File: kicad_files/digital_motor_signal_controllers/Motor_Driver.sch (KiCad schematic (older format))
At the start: 36 parts

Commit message: Code and PCB modifications
Adjustments to DSC motor controller PCB as well as BOMs
Nearly completed cannibalization of VESC code for the DSC motor control
application.
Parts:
- added D4: TVS, SMAJ5.0A:DIOM5026X229N, symbol SMAJ5.0A:SMAJ5.0A
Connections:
- net +5V: now also D4.1
- net GND: now also D4.2
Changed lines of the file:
@@
 EESchema Schematic File Version 4
 LIBS:DSC_motor_controller-cache
-EELAYER 26 0
+EELAYER 30 0
 EELAYER END
 $Descr A4 11693 8268
@@
 U 1 1 5D363539
 P 4650 2800
-F 0 "DRV1" H 4650 4300 60  0000 C CNN
+F 0 "DRV1" H 5100 3000 60  0000 C CNN
 F 1 "DRV8302" H 5700 -350 60  0000 C CNN
 F 2 "DRV8302DCAR:SOP50P810X120-57N" H 4650 2800 60  0001 C CNN
@@
 Wire Wire Line
 	7550 3900 8900 3900
+$Comp
+L SMAJ5.0A:SMAJ5.0A D4
+U 1 1 5DB014FF
+P 1900 4350
+F 0 "D4" V 2154 4478 50  0000 L CNN
+F 1 "TVS" V 2245 4478 50  0000 L CNN
+F 2 "SMAJ5.0A:DIOM5026X229N" H 2300 4500 50  0001 L BNN
+F 3 "https://componentsearchengine.com/Datasheets/1/SMAJ5.0A.pdf" H 2300 4400 50  0001 L BNN
+F 4 "Littelfuse SMAJ5.0A, Uni-Directional TVS Diode, 400W, 2-Pin DO-214AC" H 2300 4300 50  0001 L BNN "Description"
+F 5 "2.29" H 2300 4200 50  0001 L BNN "Height"
+F 6 "576-SMAJ5.0A" H 2300 4100 50  0001 L BNN "Mouser Part Number"
+F 7 "https://www.mouser.com/Search/Refine.aspx?Keyword=576-SMAJ5.0A" H 2300 4000 50  0001 L BNN "Mouser Price/Stock"
+F 8 "LITTELFUSE" H 2300 3900 50  0001 L BNN "Manufacturer_Name"
+F 9 "SMAJ5.0A" H 2300 3800 50  0001 L BNN "Manufacturer_Part_Number"
+	1    1900 4350
+	0    1    1    0
+$EndComp
+$Comp
+L power:GND #PWR0161
+U 1 1 5DB020E3
+P 1900 4950
+F 0 "#PWR0161" H 1900 4700 50  0001 C CNN
+F 1 "GND" H 1905 4777 50  0000 C CNN
+F 2 "" H 1900 4950 50  0001 C CNN
+F 3 "" H 1900 4950 50  0001 C CNN
+	1    1900 4950
+	1    0    0    -1
+$EndComp
+$Comp
+L power:+5V #PWR0162
+U 1 1 5DB048F9
+P 1900 4350
+F 0 "#PWR0162" H 1900 4200 50  0001 C CNN
+F 1 "+5V" H 1915 4523 50  0000 C CNN
+F 2 "" H 1900 4350 60  0000 C CNN
+F 3 "" H 1900 4350 60  0000 C CNN
+	1    1900 4350
+	1    0    0    -1
+$EndComp
 $EndSCHEMATC

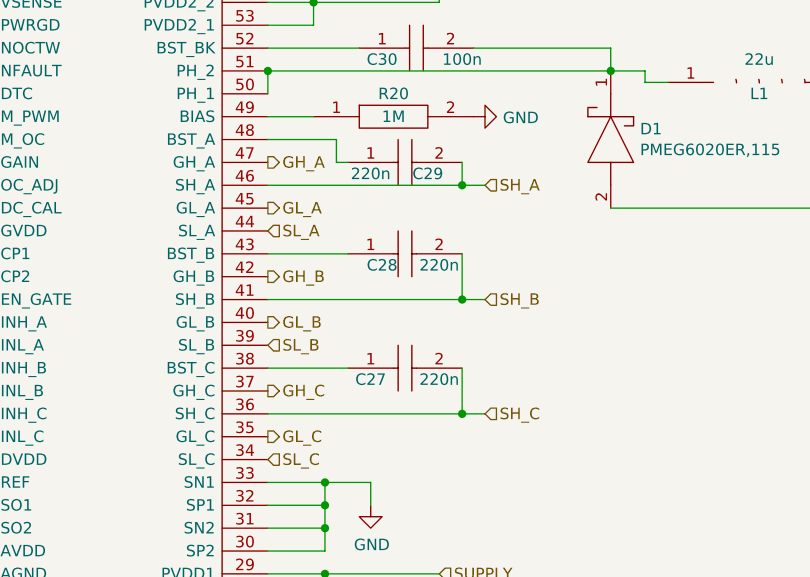
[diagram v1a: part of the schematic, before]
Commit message: replaced 220nf resistor with component that fit, moved silkscreen around, updated BOM
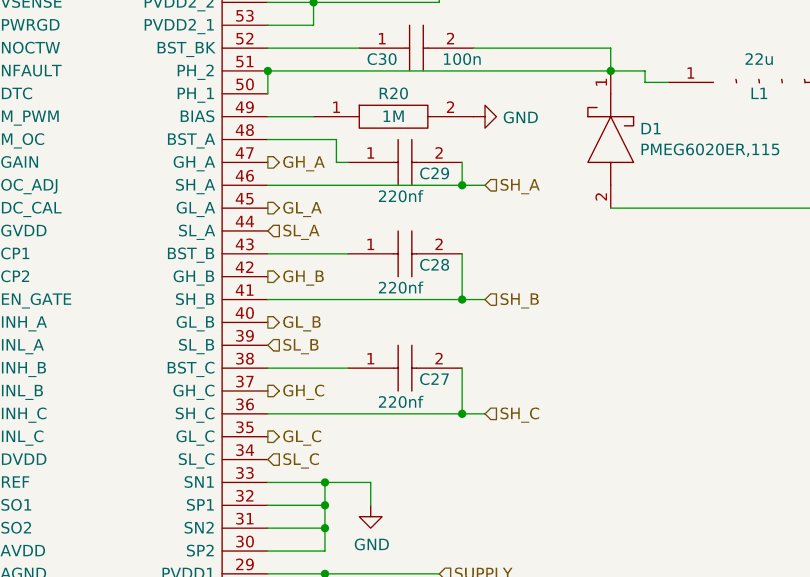
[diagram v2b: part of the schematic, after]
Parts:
- removed C27, C28, C29: 220n, GRM155C91C105ME11J:CAPC1005X55N, symbol CGA2B3X7R1E224K050BE:CGA2B3X7R1E224K050BE
- added C27, C28, C29: 220nf, GRM033R61E224KE01D:CAPC0603X33N, symbol GRM033R61E224KE01D:GRM033R61E224KE01D
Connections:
- net SH_A: now also C29.2
- net SH_B: now also C28.2
- net SH_C: now also C27.2
- net at DRV1.38 (BST_C): now also C27.1
- net at DRV1.43 (BST_B): now also C28.1
- net at DRV1.48 (BST_A): now also C29.1
